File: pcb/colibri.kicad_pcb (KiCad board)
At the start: 2 copper layers, 160 x 94.7 mm, 91 parts

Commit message: better connections
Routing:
- net lrow4: track 105.5 -> 80.4 mm
- net lcol5: track 84.1 -> 80.2 mm
- net lcol2: track 83.5 -> 79.8 mm
- net lcol1: track 84.6 -> 82.1 mm, vias 6 -> 8
- net lrow3: track 151.7 -> 153.8 mm
- net lrow2: track 146.7 -> 148.7 mm
- net lrow1: track 143.7 -> 145.3 mm
- net lcol3: track 78.7 -> 77.8 mm

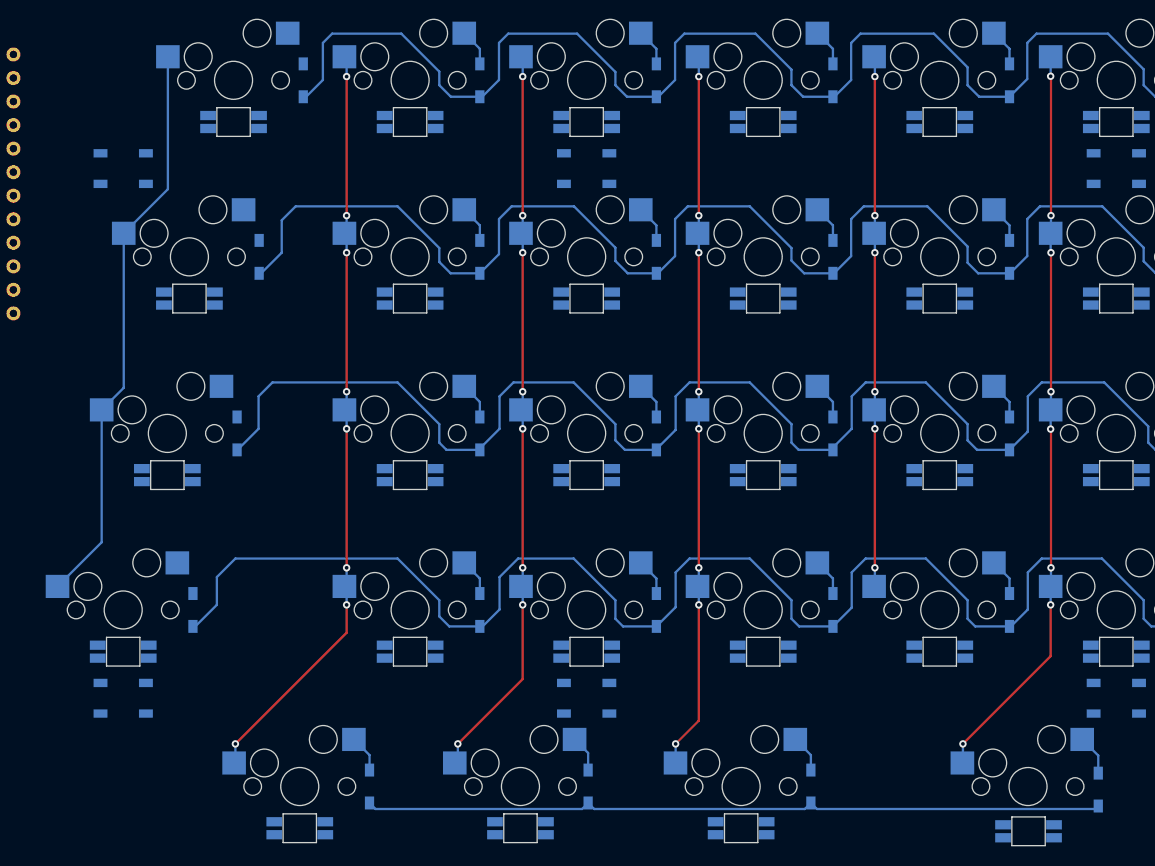
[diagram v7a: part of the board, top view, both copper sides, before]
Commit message: added missing column
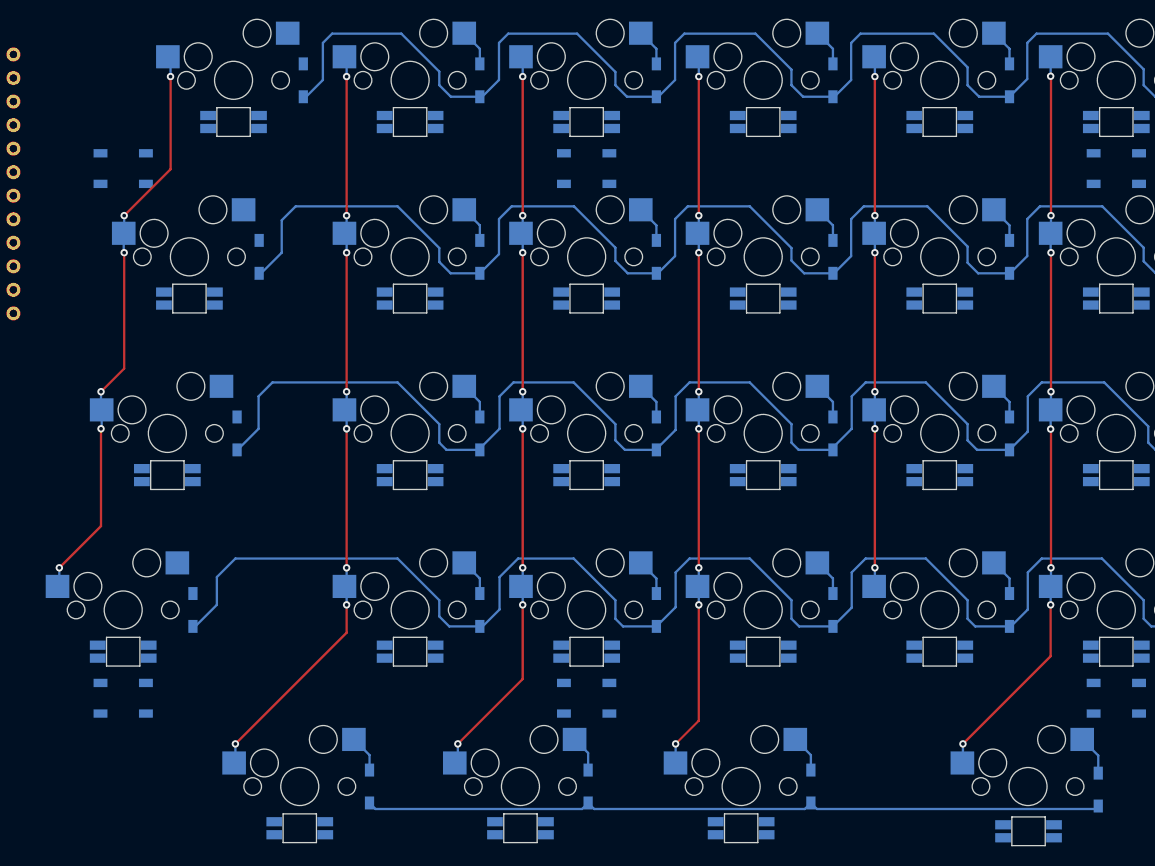
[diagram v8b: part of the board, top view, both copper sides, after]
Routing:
- net lcol1: track 82.1 -> 79.4 mm
- net lcol2: track 79.8 -> 77.5 mm
- net lcol3: track 77.8 -> 76.3 mm
- net lcol0: track 62.1 -> 63.3 mm, vias 0 -> 6
- net lcol4: track 57.4 -> 56.6 mm
- net lrow3: track 153.8 -> 153.1 mm
- net lrow4: track 80.4 -> 79.7 mm
- net lrow2: track 148.7 -> 148.2 mm
